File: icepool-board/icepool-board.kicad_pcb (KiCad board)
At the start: 4 copper layers, 90 x 40 mm, 101 parts, among them J1 PWR, J2 PWR_IN, J3 I2C, J4 SWD, J5 8P8C_Shielded, J6 8P8C_Shielded, SW1 B3U-1000P, U1 LD1117S33CTR, U2 LD1117S12CTR, U3 ATSAMD21E, U4 ISL83488/ISL83490, U5 iCE40HX8K-BG121(121-Ball_caBG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, U6 iCE40HX8K-BG121(121-Ball_caBG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, X1 ASV-12.000MHz-L??-50, Y1 16MHz

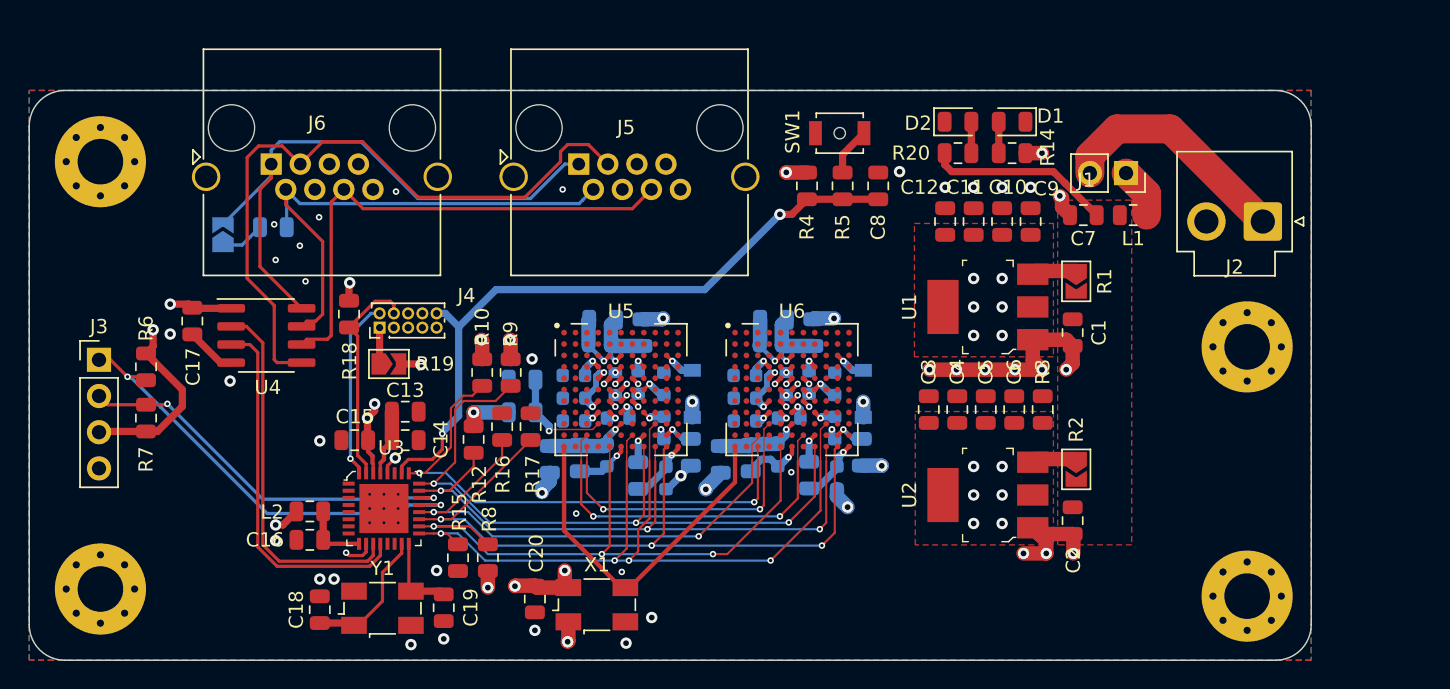
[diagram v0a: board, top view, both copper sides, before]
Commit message: Moderate rework.
* Added USB.
* Moved around SERCOMs to accommodate USB.
* Moved power connector to another edge.
* Updated FPGA oscillator model/footprint.
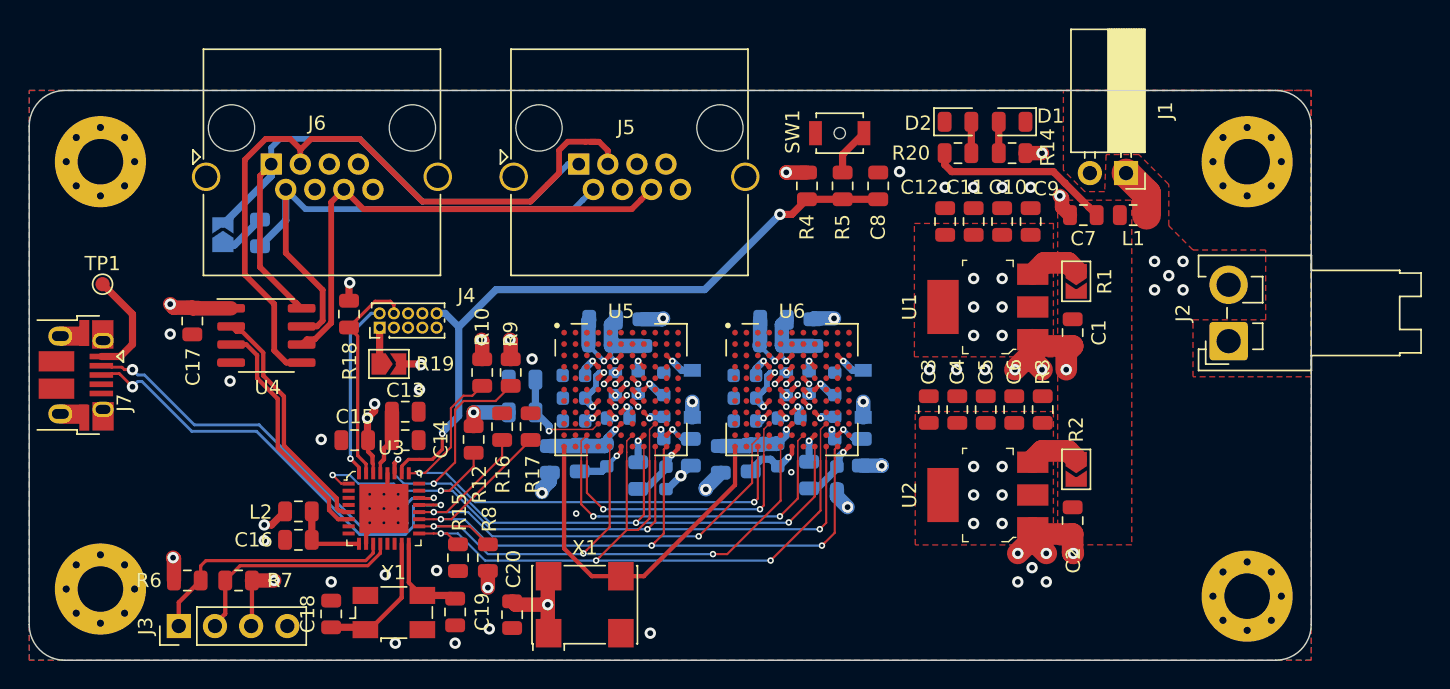
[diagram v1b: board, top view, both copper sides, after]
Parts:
- added J7: USB_B_Micro, Connector_USB:USB_Micro-B_Amphenol_10103594-0001LF_Horizontal, F.Cu at (33.3, 100.0)
- added TP1: VBUS, TestPoint:TestPoint_Pad_D1.0mm, F.Cu at (35.1, 93.6)
- J1: footprint Connector_PinSocket_2.54mm:PinSocket_1x02_P2.54mm_Vertical -> Connector_PinSocket_2.54mm:PinSocket_1x02_P2.54mm_Horizontal
- J2: footprint Connector_JST:JST_VH_B2P-VH_1x02_P3.96mm_Vertical -> Connector_JST:JST_VH_S2P-VH_1x02_P3.96mm_Horizontal
- R25, R26, R29, R30: value 10k -> 4k7
- X1: value ASV-12.000MHz-L??-50 -> CB3LV-3I-16M0000; footprint Crystal:Crystal_SMD_Abracon_ABM3B-4Pin_5.0x3.2mm -> Oscillator:Oscillator_SMD_Abracon_ASV-4Pin_7.0x5.1mm
- moved H4 30.5 mm to (115.5, 85.0)
- moved J3 19.5 mm to (40.5, 117.6), turned to 90 degrees
- moved H3 17.5 mm to (115.5, 115.5)
- moved R6 15.3 mm to (41.1, 114.4), turned to 0 degrees
- moved R7 13.1 mm to (44.7, 114.4), turned to 180 degrees
- moved J2 8.74 mm to (114.2, 97.6), turned to 90 degrees
- moved C20 1.94 mm to (63.9, 116.8)
- moved R21 1.02 mm to (46.2, 90.0), turned to 270 degrees
- moved Y1 0.85 mm to (55.6, 116.7)
- moved C18 0.85 mm to (51.2, 116.8)
- moved C19 0.85 mm to (59.9, 116.6)
- moved X1 0.85 mm to (69.0, 116.1)
- moved C16 0.80 mm to (48.9, 111.5)
- moved L2 0.80 mm to (48.9, 109.5)
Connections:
- net /SWDCLK_TCK renamed /SWD_CLK
- net /SWDIO_TMS renamed /SWD_IO
- net /TDI renamed Net-(J4-Pad8)
- net /TDO renamed Net-(J4-Pad6)
- U3 pad 1: Net-(U3-Pad1) -> /CRESET_B
- U3 pad 11: /RX -> /SDA
- U3 pad 12: /TX -> /SCL
- U3 pad 21: /SDA -> /USB_D+
- U3 pad 22: /SCL -> /USB_D-
- U3 pad 23: /CRESET_B -> Net-(U3-Pad23)
- U3 pad 24: /~GS -> Net-(U3-Pad24)
- U3 pad 27: Net-(U3-Pad27) -> /~GS
- U3 pad 33: (no net) -> GND
- U3 pad 5: Net-(U3-Pad5) -> /RX
- U3 pad 6: Net-(U3-Pad6) -> /TX
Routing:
- net /USB_D+: track 0.00 -> 32.1 mm, vias 0 -> 2
- net /USB_D-: track 0.00 -> 30.8 mm, vias 0 -> 2
- net /VPWR: track 16.8 -> 0.00 mm
- net /SDA: track 31.6 -> 18.0 mm, vias 2 -> 0
- net /SCL: track 27.6 -> 15.8 mm, vias 2 -> 0
- net /TX: track 26.1 -> 16.7 mm
- net /RX: track 26.1 -> 17.0 mm
- net /CRESET_B: track 45.2 -> 53.1 mm, vias 3 -> 4
- net Net-(J7-Pad1): track 0.00 -> 7.63 mm
- net +3V3: track 71.5 -> 64.8 mm, vias 36 -> 35
- net GND: track 51.9 -> 47.0 mm, vias 65 -> 63
- net /~GS: track 49.2 -> 53.4 mm, vias 3 -> 4
- net /RX-: track 36.7 -> 39.4 mm
- net /TX+: track 48.0 -> 50.4 mm
- net /MOSI: track 57.9 -> 56.8 mm, vias 4 -> 3
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- added copper zone on F.Cu, net /VPWR

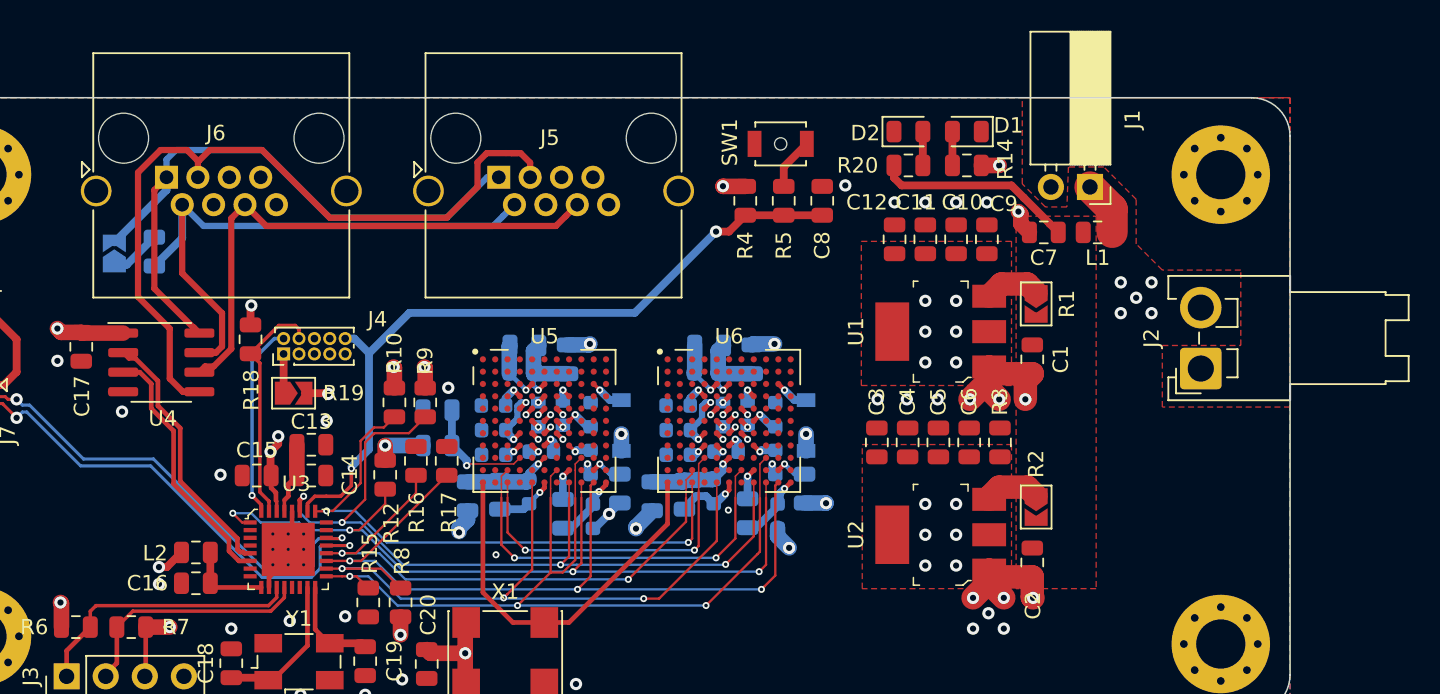
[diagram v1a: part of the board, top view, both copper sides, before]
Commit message: Changed power switch. Removed overhanging silks.
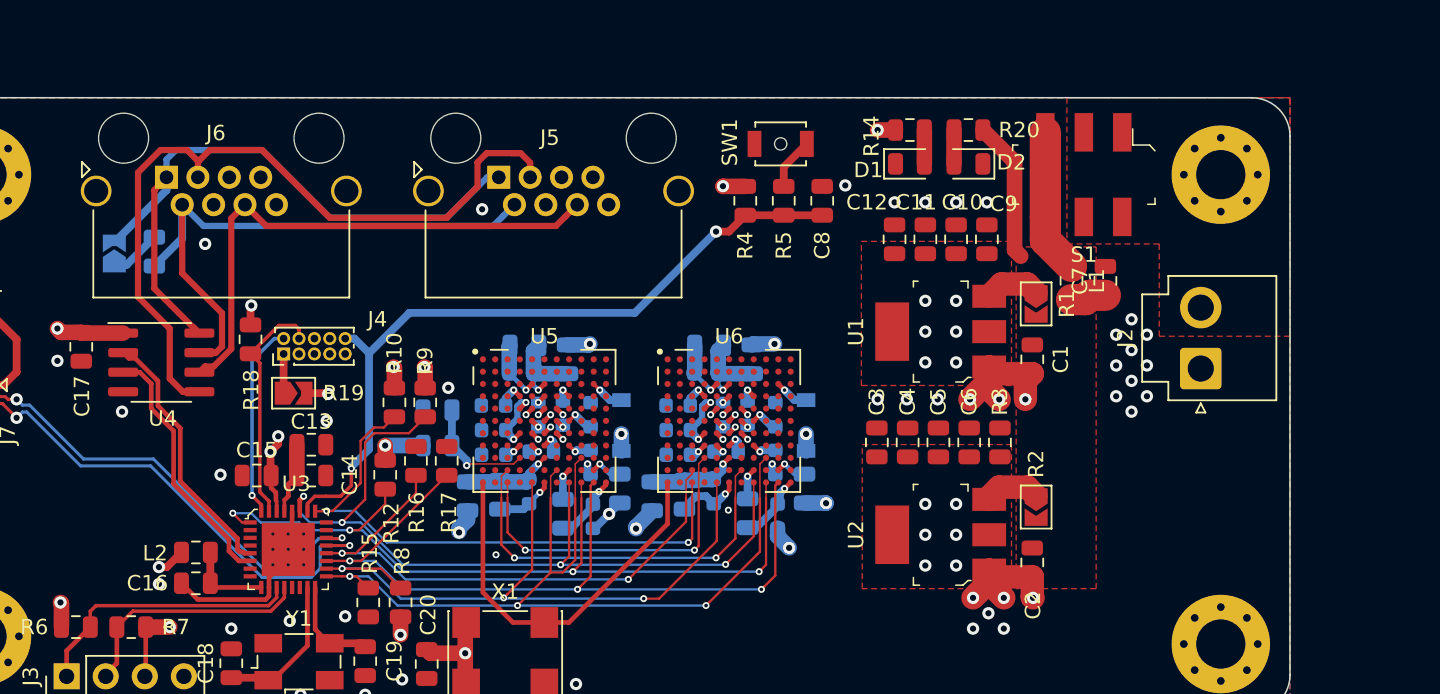
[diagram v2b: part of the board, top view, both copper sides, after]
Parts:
- removed J1: PWR, Connector_PinSocket_2.54mm:PinSocket_1x02_P2.54mm_Horizontal
- added S1: JS202011SCQN, digikey-footprints:Switch_Slide_JS202011SCQN, F.Cu at (106.6, 85.0)
- J2: footprint Connector_JST:JST_VH_S2P-VH_1x02_P3.96mm_Horizontal -> Connector_JST:JST_VH_B2P-VH-B_1x02_P3.96mm_Vertical
- J5, J6: footprint Connector_RJ:RJ45_Amphenol_RJHSE5380 -> icepool-library:RJ45_Amphenol_RJHSE5380
- moved C7 5.09 mm to (108.0, 91.9), turned to 90 degrees
- moved R20 4.53 mm to (99.1, 82.1), turned to 180 degrees
- moved D2 4.43 mm to (99.1, 84.3), turned to 180 degrees
- moved R14 4.36 mm to (95.3, 82.1), turned to 0 degrees
- moved D1 4.25 mm to (95.3, 84.3), turned to 0 degrees
- moved L1 3.58 mm to (105.8, 91.9), turned to 270 degrees
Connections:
- J2 pad 1: /VPWR -> GND
- J2 pad 2: GND -> /VPWR
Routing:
- net Net-(L1-Pad1): track 3.55 -> 9.42 mm
- net GND: track 47.0 -> 52.1 mm, vias 63 -> 69
- net VCC: track 13.0 -> 11.5 mm
